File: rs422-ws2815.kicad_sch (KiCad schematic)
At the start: 32 parts, among them J1 12V, J10 DO, J11 DI, J12 GND, J13 +5V OUT, J2 12V, J3 12V, J4 A, J5 B, J6 GND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

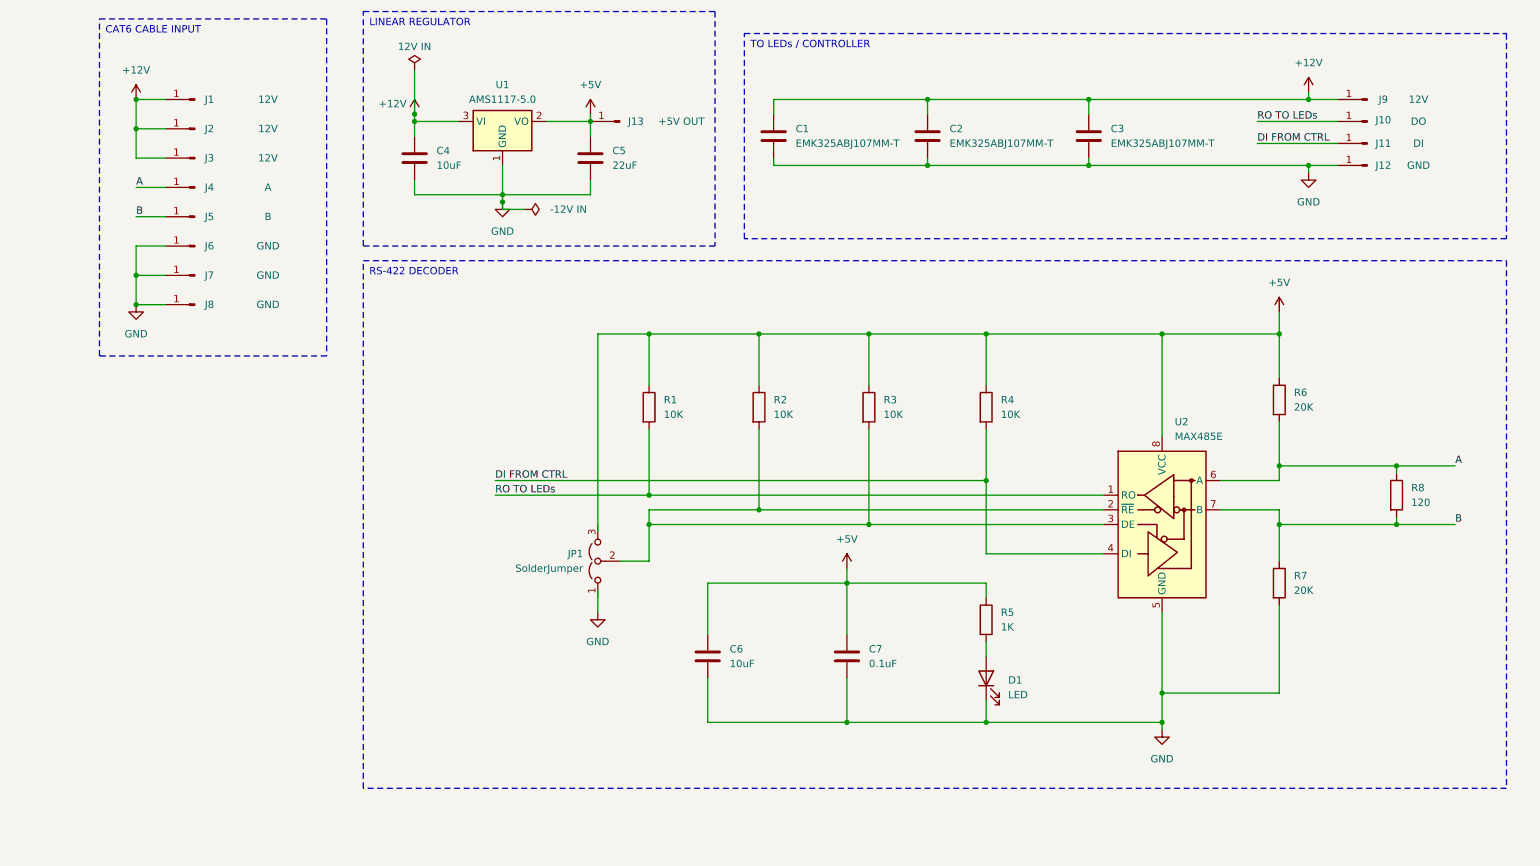
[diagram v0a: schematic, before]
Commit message: Add files via upload
Changed to TI TLV761 5V reg & updated caps to suit
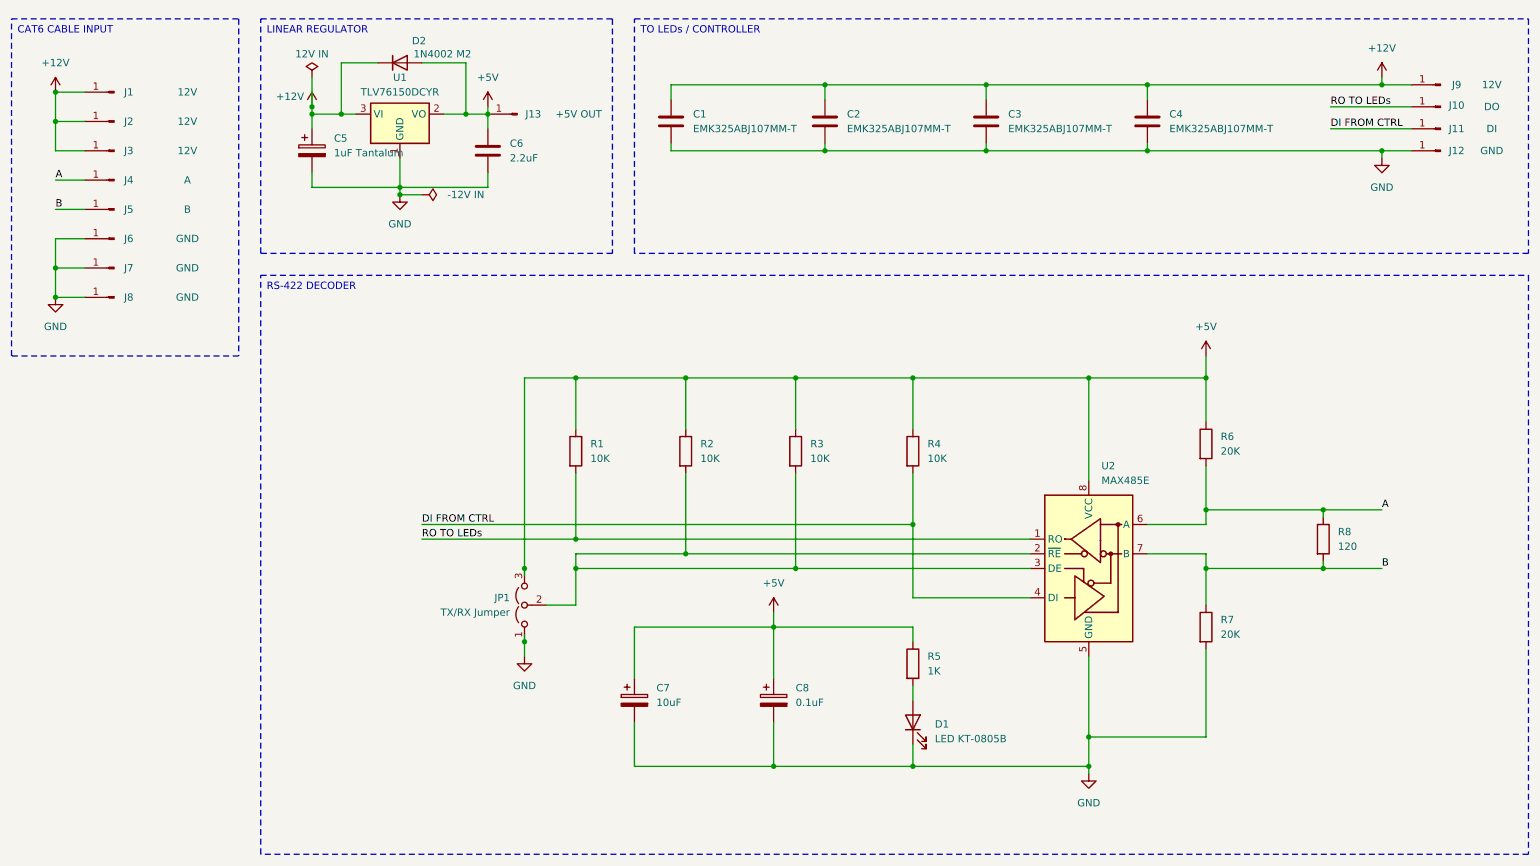
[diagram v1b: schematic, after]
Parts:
- added C4: EMK325ABJ107MM-T, Capacitor_SMD:C_1210_3225Metric, symbol Device:C
- added D2: 1N4002 M2, Diode_SMD:D_SMA, symbol Diode:1N4002
- C5: renamed from C4; value 10uF -> 1uF Tantalum; symbol Device:C -> Device:C_Polarized
- C6: renamed from C5; value 22uF -> 2.2uF
- C7: renamed from C6; symbol Device:C -> Device:C_Polarized
- C8: renamed from C7; footprint Capacitor_SMD:C_0805_2012Metric -> Capacitor_SMD:C_0603_1608Metric; symbol Device:C -> Device:C_Polarized
- D1: value LED -> LED KT-0805B
- JP1: value SolderJumper -> TX/RX Jumper; footprint Jumper:SolderJumper-3_P1.3mm_Open_RoundedPad1.0x1.5mm_NumberLabels -> Jumper:SolderJumper-3_P2.0mm_Open_TrianglePad1.0x1.5mm
- U1: value AMS1117-5.0 -> TLV76150DCYR; symbol Regulator_Linear:AMS1117-5.0 -> Regulator_Linear:TLV76150DCY
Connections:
- net +12V: now also C4.1, D2.1 (K)
- net +5V: now also JP1.3 (B), D2.2 (A)
- net GND: now also JP1.1 (A), C4.2
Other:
- moved on the sheet: C1, C2, C3, C6, D1, J1, J10, J11, J12, J13, J2, J3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
